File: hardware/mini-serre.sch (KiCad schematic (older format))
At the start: 40 parts, among them J0 POWER, J1 SERIAL, J2 ACT, J3 SEN, J4 I2C, J5 EXT, Q1 IMH20TR1G, Q2 VNN3NV04PTR, Q3 VNN3NV04PTR, Q4 VNN3NV04PTR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

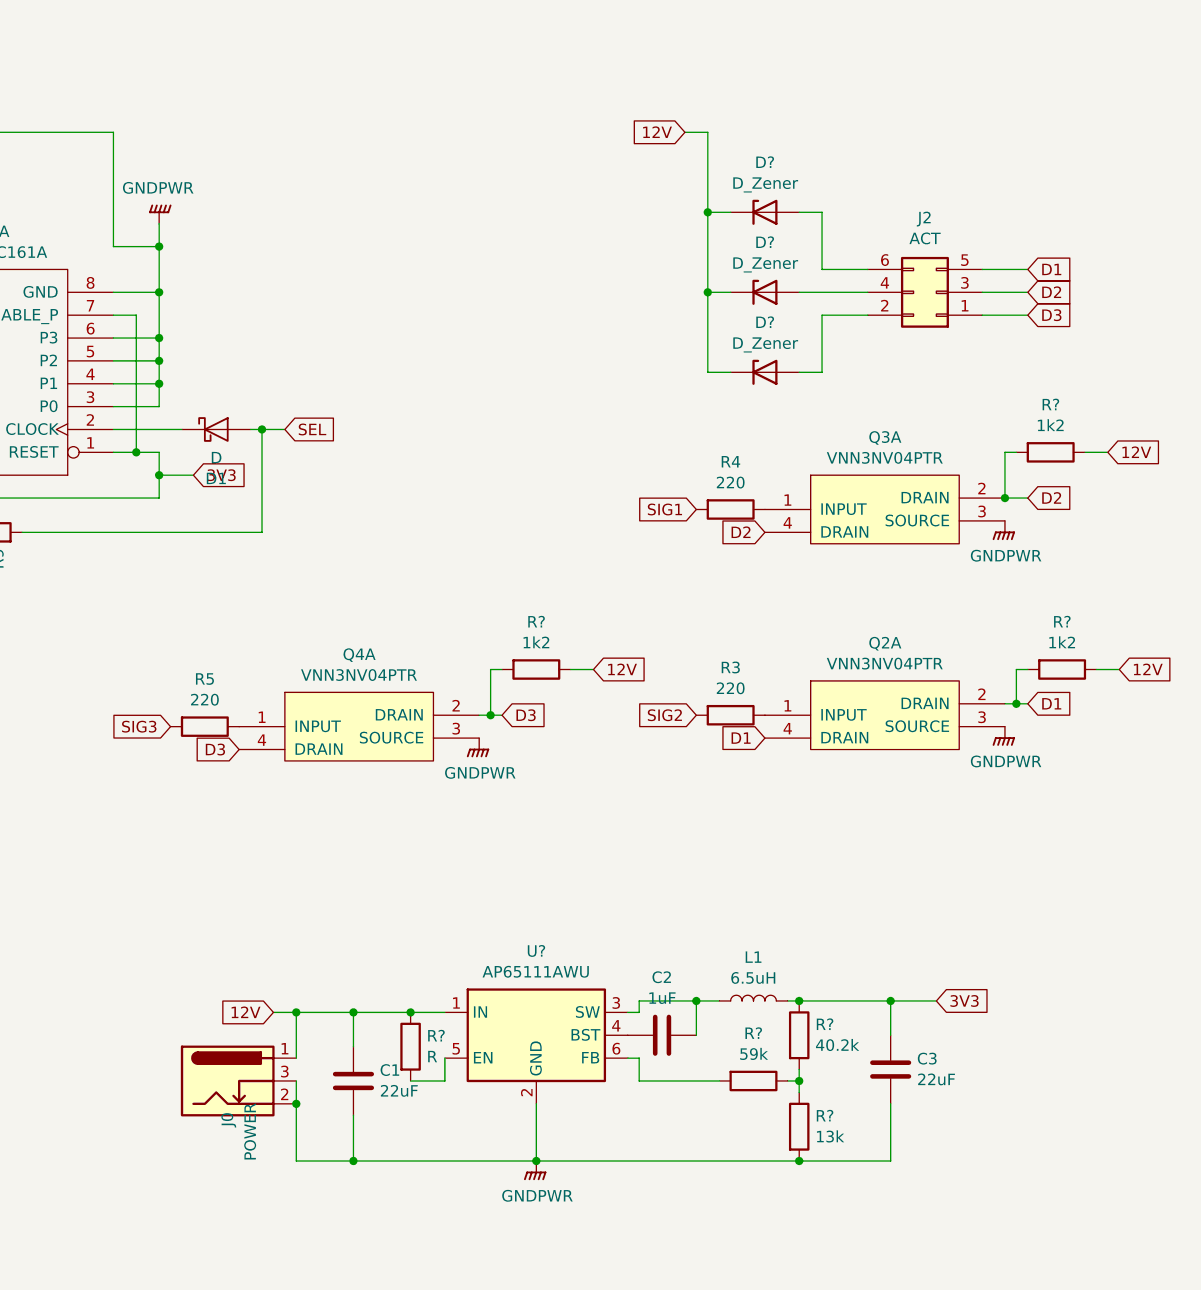
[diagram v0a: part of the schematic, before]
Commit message: update schematics with buck converter, add part info and begin routing
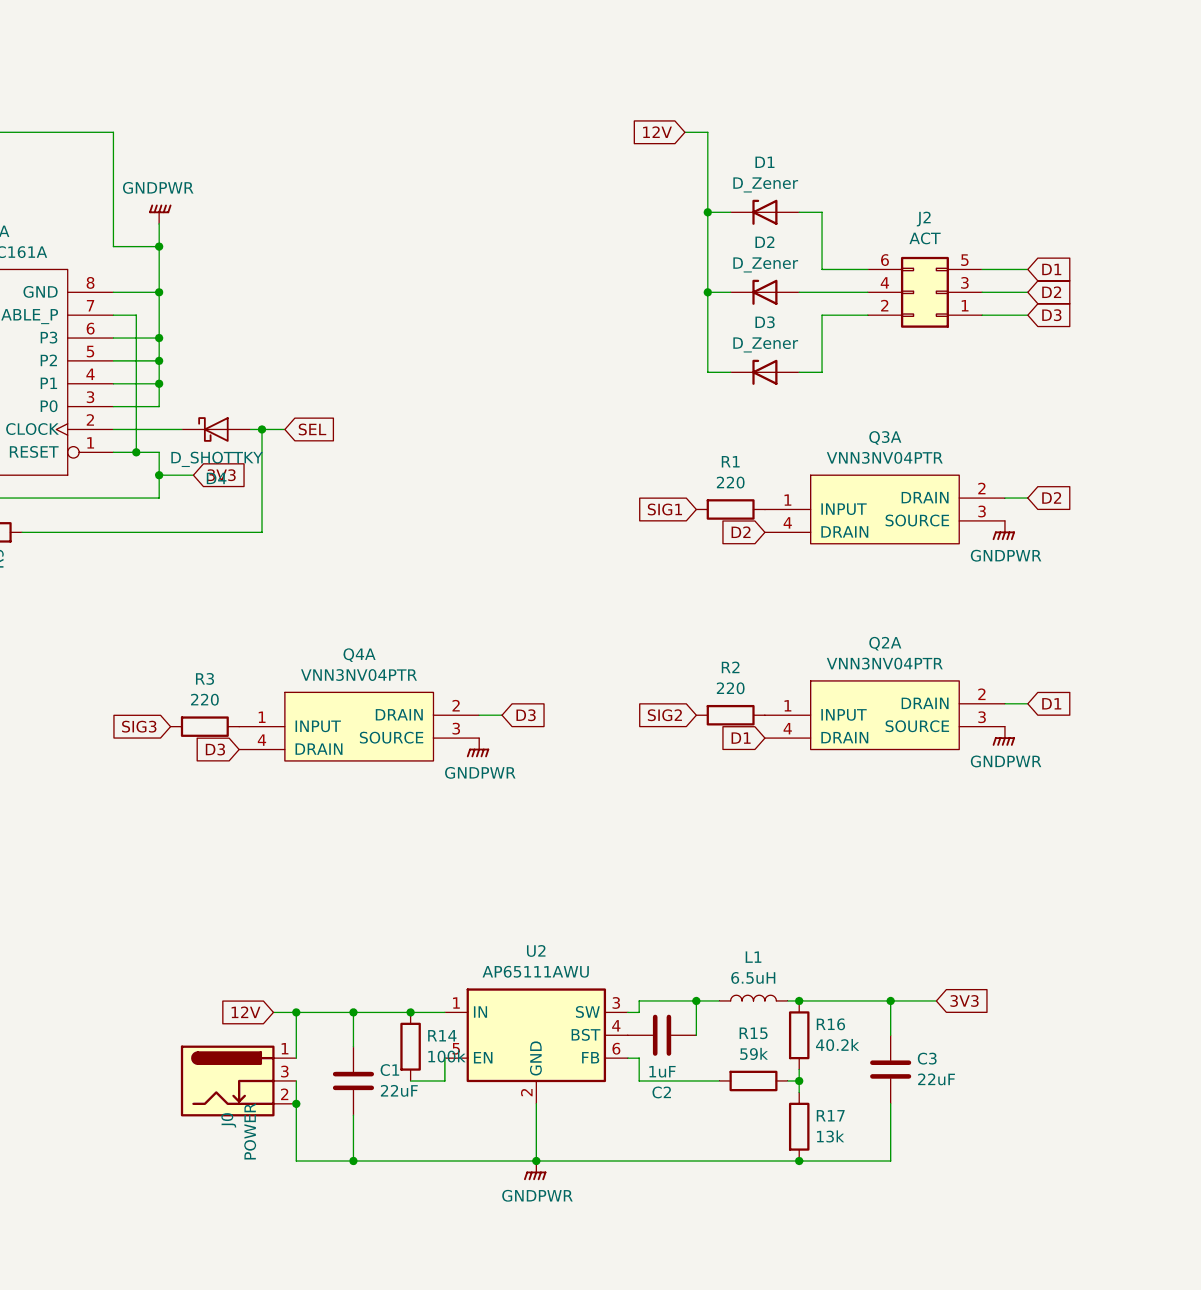
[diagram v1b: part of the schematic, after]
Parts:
- removed R? (x3): 1k2, symbol Device:R
- C1, C2, C3: footprint (none) -> Capacitor_SMD:C_1206_3216Metric_Pad1.42x1.75mm_HandSolder
- D1, D2, D3: renamed from D?; footprint (none) -> Diode_SMD:D_SMA_Handsoldering; Mouser (none) -> 78-BZG05C5V6-M3-08
- D4: renamed from D1; value D -> D_SHOTTKY; footprint (none) -> Diode_SMD:D_SOD-123
- L1: footprint (none) -> Inductor_SMD:L_Taiyo-Yuden_NR-10050_9.8x10.0mm_HandSoldering; Mouser (none) -> 963-NR10050T6R5N
- R14: renamed from R?; value R -> 100k; footprint (none) -> Resistor_SMD:R_1206_3216Metric_Pad1.42x1.75mm_HandSolder; Mouser (none) -> 71-CRCW1206100KFKEAC
- R15: renamed from R?; footprint (none) -> Resistor_SMD:R_1206_3216Metric_Pad1.42x1.75mm_HandSolder; Mouser (none) -> 667-ERJ-8ENF5902V
- R16: renamed from R?; footprint (none) -> Resistor_SMD:R_1206_3216Metric_Pad1.42x1.75mm_HandSolder; Mouser (none) -> 652-CR1206FX-4022ELF
- R17: renamed from R?; footprint (none) -> Resistor_SMD:R_1206_3216Metric_Pad1.42x1.75mm_HandSolder; Mouser (none) -> 667-ERJ-8ENF1302V
- gave numbers to parts that had none: 1
- renumbered R4 to R1, R3 to R2, R5 to R3
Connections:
- net at L1.1, U2.3 (SW): now also C2.1; no longer C2.2
- net at U2.4 (BST): now also C2.2; no longer C2.1
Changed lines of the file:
@@
 $EndComp
 $Comp
-L mini-serre-rescue:R-Device R4
+L mini-serre-rescue:R-Device R1
 U 1 1 5E6C97A0
 P 9100 2650
-F 0 "R4" V 8893 2650 50  0000 C CNN
+F 0 "R1" V 8893 2650 50  0000 C CNN
 F 1 "220" V 8984 2650 50  0000 C CNN
 F 2 "Resistor_SMD:R_1210_3225Metric_Pad1.42x2.65mm_HandSolder" V 9030 2650 50  0001 C CNN
@@
 $EndComp
 $Comp
-L mini-serre-rescue:R-Device R5
+L mini-serre-rescue:R-Device R3
 U 1 1 5E7F839A
 P 6800 3600
-F 0 "R5" V 6593 3600 50  0000 C CNN
+F 0 "R3" V 6593 3600 50  0000 C CNN
 F 1 "220" V 6684 3600 50  0000 C CNN
 F 2 "Resistor_SMD:R_1210_3225Metric_Pad1.42x2.65mm_HandSolder" V 6730 3600 50  0001 C CNN
@@
 $EndComp
 $Comp
-L mini-serre-rescue:R-Device R3
+L mini-serre-rescue:R-Device R2
 U 1 1 5E83B7A0
 P 9100 3550
-F 0 "R3" V 8893 3550 50  0000 C CNN
+F 0 "R2" V 8893 3550 50  0000 C CNN
 F 1 "220" V 8984 3550 50  0000 C CNN
 F 2 "Resistor_SMD:R_1210_3225Metric_Pad1.42x2.65mm_HandSolder" V 9030 3550 50  0001 C CNN
@@
 $EndComp
 $Comp
-L mini-serre-rescue:D_Schottky-Device D1
+L mini-serre-rescue:D_Schottky-Device D4
 U 1 1 5E954EFD
 P 6850 2300
-F 0 "D1" H 6850 2084 50  0000 C CNN
-F 1 "D" H 6850 2175 50  0000 C CNN
-F 2 "" H 6850 2300 50  0001 C CNN
-F 3 "~" H 6850 2300 50  0001 C CNN
+F 0 "D4" H 6850 2084 50  0000 C CNN
+F 1 "D_SHOTTKY" H 6850 2175 50  0000 C CNN
+F 2 "Diode_SMD:D_SOD-123" H 6850 2300 50  0001 C CNN
+F 3 "https://shop.boxtec.ch/pub/diverse/ds30217.pdf" H 6850 2300 50  0001 C CNN
 	1    6850 2300
 	1    0    0    -1
@@
 	6400 2300 6700 2300
 $Comp
-L Regulator_Switching:AP65111AWU U?
+L Regulator_Switching:AP65111AWU U2
 U 1 1 5EACE685
 P 8250 4950
-F 0 "U?" H 8250 5317 50  0000 C CNN
+F 0 "U2" H 8250 5317 50  0000 C CNN
 F 1 "AP65111AWU" H 8250 5226 50  0000 C CNN
 F 2 "Package_TO_SOT_SMD:TSOT-23-6" H 8250 4050 50  0001 C CNN
@@
 F 0 "L1" V 9390 4800 50  0000 C CNN
 F 1 "6.5uH" V 9299 4800 50  0000 C CNN
-F 2 "" H 9200 4800 50  0001 C CNN
-F 3 "~" H 9200 4800 50  0001 C CNN
+F 2 "Inductor_SMD:L_Taiyo-Yuden_NR-10050_9.8x10.0mm_HandSoldering" H 9200 4800 50  0001 C CNN
+F 3 "https://www.mouser.ch/datasheet/2/396/wound06_e-1313806.pdf" H 9200 4800 50  0001 C CNN
+F 4 "963-NR10050T6R5N" V 9200 4800 50  0001 C CNN "Mouser"
 	1    9200 4800
 	0    -1   -1   0
@@
 F 0 "C2" V 9052 4950 50  0000 C CNN
 F 1 "1uF" V 8961 4950 50  0000 C CNN
-F 2 "" H 8838 4800 50  0001 C CNN
-F 3 "~" H 8800 4950 50  0001 C CNN
+F 2 "Capacitor_SMD:C_1206_3216Metric_Pad1.42x1.75mm_HandSolder" H 8838 4800 50  0001 C CNN
+F 3 "https://www.mouser.ch/datasheet/2/212/KEM_C1006_X5R_SMD-1103249.pdf" H 8800 4950 50  0001 C CNN
 	1    8800 4950
-	0    -1   -1   0
+	0    1    1    0
 $EndComp
 $Comp
@@
 F 0 "C3" H 9915 5146 50  0000 L CNN
 F 1 "22uF" H 9915 5055 50  0000 L CNN
-F 2 "" H 9838 4950 50  0001 C CNN
-F 3 "~" H 9800 5100 50  0001 C CNN
+F 2 "Capacitor_SMD:C_1206_3216Metric_Pad1.42x1.75mm_HandSolder" H 9838 4950 50  0001 C CNN
+F 3 "https://www.mouser.ch/datasheet/2/212/KEM_C1006_X5R_SMD-1103249.pdf" H 9800 5100 50  0001 C CNN
 	1    9800 5100
 	1    0    0    -1
@@
 F 0 "C1" H 7565 5196 50  0000 L CNN
 F 1 "22uF" H 7565 5105 50  0000 L CNN
-F 2 "" H 7488 5000 50  0001 C CNN
-F 3 "~" H 7450 5150 50  0001 C CNN
+F 2 "Capacitor_SMD:C_1206_3216Metric_Pad1.42x1.75mm_HandSolder" H 7488 5000 50  0001 C CNN
+F 3 "https://www.mouser.ch/datasheet/2/212/KEM_C1006_X5R_SMD-1103249.pdf" H 7450 5150 50  0001 C CNN
 	1    7450 5150
 	1    0    0    -1
 $EndComp
 $Comp
-L Device:R R?
+L Device:R R16
 U 1 1 5EAD77D8
 P 9400 4950
-F 0 "R?" H 9470 4996 50  0000 L CNN
+F 0 "R16" H 9470 4996 50  0000 L CNN
 F 1 "40.2k" H 9470 4905 50  0000 L CNN
-F 2 "" V 9330 4950 50  0001 C CNN
-F 3 "~" H 9400 4950 50  0001 C CNN
+F 2 "Resistor_SMD:R_1206_3216Metric_Pad1.42x1.75mm_HandSolder" V 9330 4950 50  0001 C CNN
+F 3 "https://www.mouser.ch/datasheet/2/54/chpreztr-777398.pdf" H 9400 4950 50  0001 C CNN
+F 4 "652-CR1206FX-4022ELF " H 9400 4950 50  0001 C CNN "Mouser"
 	1    9400 4950
 	1    0    0    -1
 $EndComp
 $Comp
-L Device:R R?
+L Device:R R15
 U 1 1 5EAD830B
 P 9200 5150
-F 0 "R?" V 8993 5150 50  0000 C CNN
+F 0 "R15" V 8993 5150 50  0000 C CNN
 F 1 "59k" V 9084 5150 50  0000 C CNN
-F 2 "" V 9130 5150 50  0001 C CNN
-F 3 "~" H 9200 5150 50  0001 C CNN
+F 2 "Resistor_SMD:R_1206_3216Metric_Pad1.42x1.75mm_HandSolder" V 9130 5150 50  0001 C CNN
+F 3 "https://www.mouser.ch/datasheet/2/315/AOA0000C304-1149620.pdf" H 9200 5150 50  0001 C CNN
+F 4 "667-ERJ-8ENF5902V" V 9200 5150 50  0001 C CNN "Mouser"
 	1    9200 5150
 	0    1    1    0
 $EndComp
 $Comp
-L Device:R R?
+L Device:R R17
 U 1 1 5EAD8B39
 P 9400 5350
-F 0 "R?" H 9470 5396 50  0000 L CNN
+F 0 "R17" H 9470 5396 50  0000 L CNN
 F 1 "13k" H 9470 5305 50  0000 L CNN
-F 2 "" V 9330 5350 50  0001 C CNN
-F 3 "~" H 9400 5350 50  0001 C CNN
+F 2 "Resistor_SMD:R_1206_3216Metric_Pad1.42x1.75mm_HandSolder" V 9330 5350 50  0001 C CNN
+F 3 "https://www.mouser.ch/datasheet/2/315/AOA0000C304-1149620.pdf" H 9400 5350 50  0001 C CNN
+F 4 "667-ERJ-8ENF1302V " H 9400 5350 50  0001 C CNN "Mouser"
 	1    9400 5350
 	1    0    0    -1
@@
 Wire Wire Line
 	8700 4850 8700 4800
-Wire Wire Line
-	8700 4800 8950 4800
 Wire Wire Line
 	8950 4950 8950 4800
@@
 Connection ~ 7200 4850
 $Comp
-L Device:D_Zener D?
+L Device:D_Zener D1
 U 1 1 5F04AB6D
 P 9250 1350
-F 0 "D?" H 9250 1567 50  0000 C CNN
+F 0 "D1" H 9250 1567 50  0000 C CNN
 F 1 "D_Zener" H 9250 1476 50  0000 C CNN
-F 2 "" H 9250 1350 50  0001 C CNN
-F 3 "~" H 9250 1350 50  0001 C CNN
+F 2 "Diode_SMD:D_SMA_Handsoldering" H 9250 1350 50  0001 C CNN
+F 3 "https://www.mouser.ch/datasheet/2/427/bzg05c-m-series-1767829.pdf" H 9250 1350 50  0001 C CNN
+F 4 "78-BZG05C5V6-M3-08 " H 9250 1350 50  0001 C CNN "Mouser"
 	1    9250 1350
 	1    0    0    -1
 $EndComp
 $Comp
-L Device:D_Zener D?
+L Device:D_Zener D2
 U 1 1 5F04F779
 P 9250 1700
-F 0 "D?" H 9250 1917 50  0000 C CNN
+F 0 "D2" H 9250 1917 50  0000 C CNN
 F 1 "D_Zener" H 9250 1826 50  0000 C CNN
-F 2 "" H 9250 1700 50  0001 C CNN
-F 3 "~" H 9250 1700 50  0001 C CNN
+F 2 "Diode_SMD:D_SMA_Handsoldering" H 9250 1700 50  0001 C CNN
+F 3 "https://www.mouser.ch/datasheet/2/427/bzg05c-m-series-1767829.pdf" H 9250 1700 50  0001 C CNN
+F 4 "78-BZG05C5V6-M3-08" H 9250 1700 50  0001 C CNN "Mouser"
 	1    9250 1700
 	1    0    0    -1
 $EndComp
 $Comp
-L Device:D_Zener D?
+L Device:D_Zener D3
 U 1 1 5F051B47
 P 9250 2050
-F 0 "D?" H 9250 2267 50  0000 C CNN
+F 0 "D3" H 9250 2267 50  0000 C CNN
 F 1 "D_Zener" H 9250 2176 50  0000 C CNN
-F 2 "" H 9250 2050 50  0001 C CNN
-F 3 "~" H 9250 2050 50  0001 C CNN
+F 2 "Diode_SMD:D_SMA_Handsoldering" H 9250 2050 50  0001 C CNN
+F 3 "https://www.mouser.ch/datasheet/2/427/bzg05c-m-series-1767829.pdf" H 9250 2050 50  0001 C CNN
+F 4 "78-BZG05C5V6-M3-08 " H 9250 2050 50  0001 C CNN "Mouser"
 	1    9250 2050
 	1    0    0    -1
@@
 Wire Wire Line
 	9400 2050 9500 2050
-Text GLabel 10750 2400 2    50   Input ~ 0
-12V
-$Comp
-L Device:R R?
-U 1 1 5F1FE892
-P 10500 2400
-F 0 "R?" V 10293 2400 50  0000 C CNN
-F 1 "1k2" V 10384 2400 50  0000 C CNN
-F 2 "" V 10430 2400 50  0001 C CNN
-F 3 "~" H 10500 2400 50  0001 C CNN
-	1    10500 2400
-	0    1    1    0
-$EndComp
-Wire Wire Line
-	10750 2400 10650 2400
 Wire Wire Line
 	10300 2600 10400 2600
-Wire Wire Line
-	10350 2400 10300 2400
-Wire Wire Line
-	10300 2400 10300 2600
-Connection ~ 10300 2600
-Text GLabel 10800 3350 2    50   Input ~ 0
-12V
-$Comp
-L Device:R R?
-U 1 1 5F3022D6
-P 10550 3350
-F 0 "R?" V 10343 3350 50  0000 C CNN
-F 1 "1k2" V 10434 3350 50  0000 C CNN
-F 2 "" V 10480 3350 50  0001 C CNN
-F 3 "~" H 10550 3350 50  0001 C CNN
-	1    10550 3350
-	0    1    1    0
-$EndComp
-Wire Wire Line
-	10800 3350 10700 3350
-Wire Wire Line
-	10400 3350 10350 3350
-Text GLabel 8500 3350 2    50   Input ~ 0
-12V
-$Comp
-L Device:R R?
-U 1 1 5F312FB8
-P 8250 3350
-F 0 "R?" V 8043 3350 50  0000 C CNN
-F 1 "1k2" V 8134 3350 50  0000 C CNN
-F 2 "" V 8180 3350 50  0001 C CNN
-F 3 "~" H 8250 3350 50  0001 C CNN
-	1    8250 3350
-	0    1    1    0
-$EndComp
-Wire Wire Line
-	8500 3350 8400 3350
-Wire Wire Line
-	8100 3350 8050 3350
-Wire Wire Line
-	8100 3550 8050 3550
-Wire Wire Line
-	8050 3350 8050 3550
-Connection ~ 8050 3550
-Wire Wire Line
-	8050 3550 8000 3550
-Wire Wire Line
-	10350 3350 10350 3500
-Wire Wire Line
-	10350 3500 10300 3500
-Wire Wire Line
-	10350 3500 10400 3500
-Connection ~ 10350 3500
-$Comp
-L Device:R R?
+$Comp
+L Device:R R14
 U 1 1 5EBC3512
 P 7700 5000
-F 0 "R?" H 7770 5046 50  0000 L CNN
-F 1 "R" H 7770 4955 50  0000 L CNN
-F 2 "" V 7630 5000 50  0001 C CNN
-F 3 "~" H 7700 5000 50  0001 C CNN
+F 0 "R14" H 7770 5046 50  0000 L CNN
+F 1 "100k" H 7770 4955 50  0000 L CNN
+F 2 "Resistor_SMD:R_1206_3216Metric_Pad1.42x1.75mm_HandSolder" V 7630 5000 50  0001 C CNN
+F 3 "https://www.mouser.ch/datasheet/2/427/crcwce3-1762584.pdf" H 7700 5000 50  0001 C CNN
+F 4 "71-CRCW1206100KFKEAC" H 7700 5000 50  0001 C CNN "Mouser"
 	1    7700 5000
 	1    0    0    -1
@@
 Wire Wire Line
 	7850 5150 7850 5050
+Wire Wire Line
+	8700 4800 8950 4800
+Wire Wire Line
+	8000 3550 8100 3550
+Wire Wire Line
+	10300 3500 10400 3500
 $EndSCHEMATC
